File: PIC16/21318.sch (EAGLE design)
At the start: 11 parts, among them U2 I50115

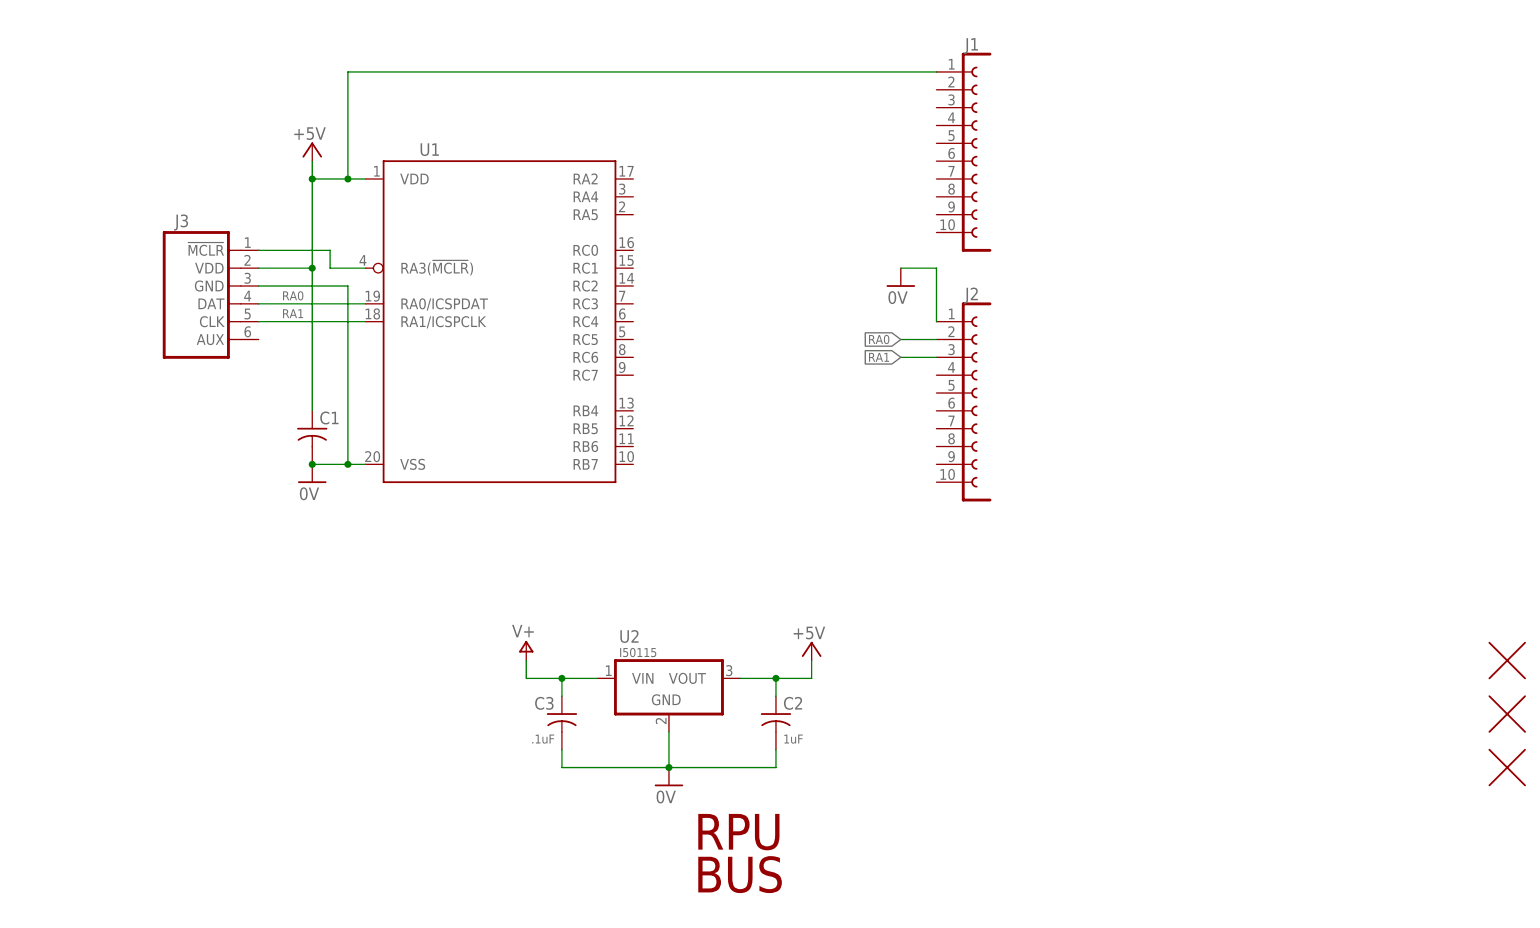
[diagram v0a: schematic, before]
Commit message: PIC16
8pin, 14pin, and 20pin will work, just keep pin 1 fixed.
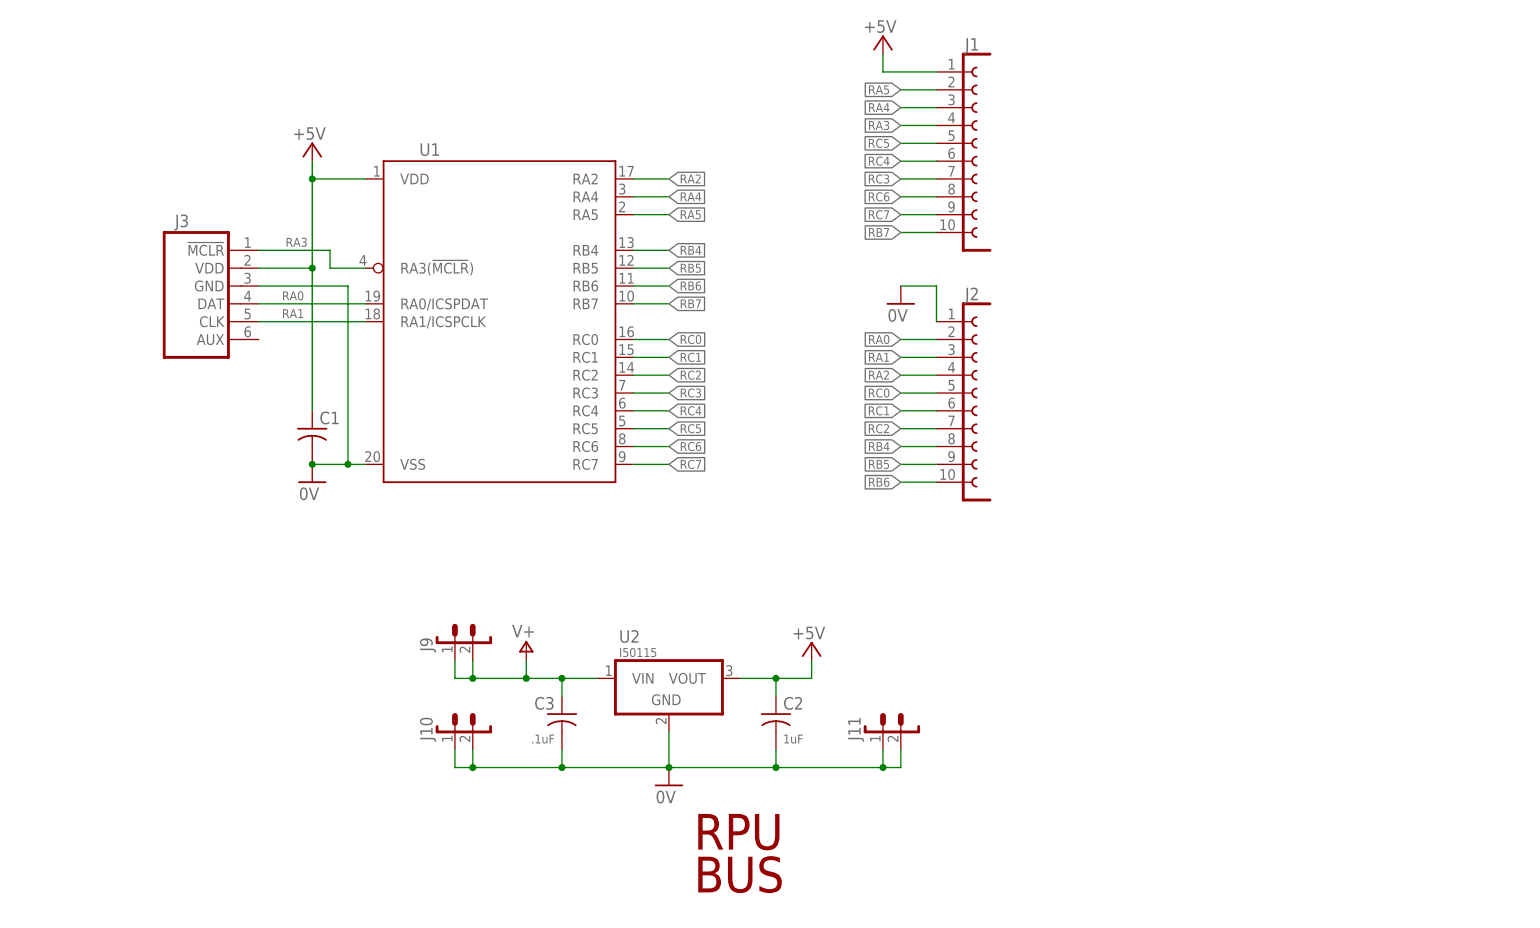
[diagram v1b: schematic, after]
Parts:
- removed U$2, U$3, U$4: FIDUCIAL1.27, H-Fiducial:FIDUCIAL1.27
- added J10, J11, J9: (no value), J-HDR2.54mm:1X2
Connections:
- removed net N$1: J3.!MCLR, U1.RA3(!MCLR!)
- new net RA2: J2.4, U1.RA2
- new net RA3: J1.4, J3.!MCLR, U1.RA3(!MCLR!)
- new net RA4: J1.3, U1.RA4
- new net RA5: J1.2, U1.RA5
- new net RB4: J2.8, U1.RB4
- new net RB5: J2.9, U1.RB5
- new net RB6: J2.10, U1.RB6
- new net RB7: J1.10, U1.RB7
- new net RC0: J2.5, U1.RC0
- new net RC1: J2.6, U1.RC1
- new net RC2: J2.7, U1.RC2
- new net RC3: J1.7, U1.RC3
- new net RC4: J1.6, U1.RC4
- new net RC5: J1.5, U1.RC5
- new net RC6: J1.8, U1.RC6
- new net RC7: J1.9, U1.RC7
- net 0V: now also J10.1, J10.2, J11.1, J11.2
- net V+: now also J9.1, J9.2

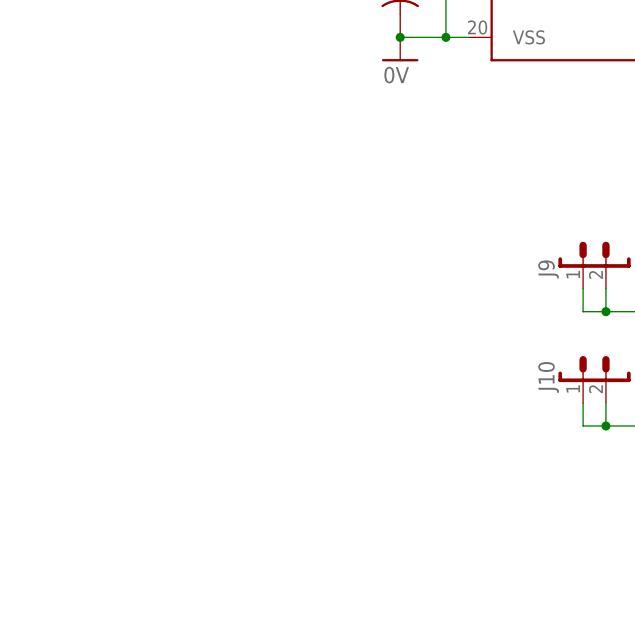
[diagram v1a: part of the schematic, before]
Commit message: PIC16: add three switches
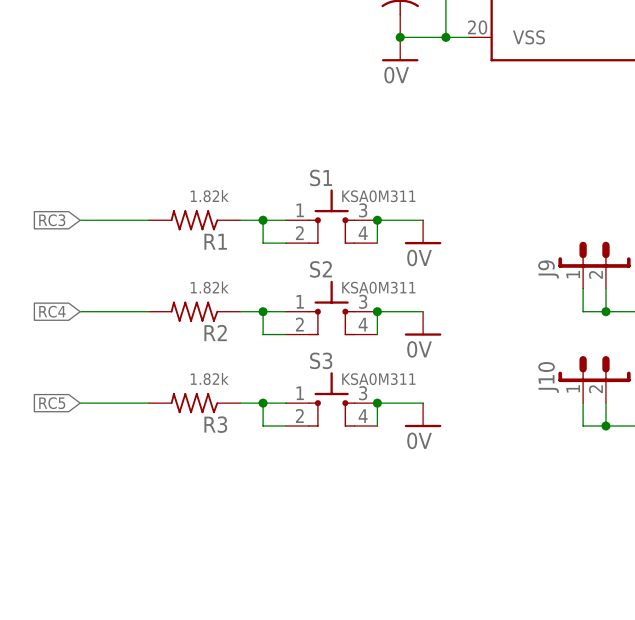
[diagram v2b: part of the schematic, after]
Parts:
- added R1, R2, R3: 1.82k, R-C:R0805
- added S1, S2, S3: KSA0M311, S-Tactile:KSA0M311
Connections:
- new net N$1: R2.1, S2.1, S2.2
- new net N$2: R3.1, S3.1, S3.2
- new net N$93: R1.1, S1.1, S1.2
- net 0V: now also S1.3, S1.4, S2.3, S2.4, S3.3, S3.4
- net RC3: now also R1.2
- net RC4: now also R2.2
- net RC5: now also R3.2
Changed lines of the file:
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@@
 <part name="J10" library="J-HDR2.54mm" deviceset="1X2" device=""/>
 <part name="J11" library="J-HDR2.54mm" deviceset="1X2" device=""/>
+<part name="S1" library="S-Tactile" deviceset="KSA" device="0M311" value="KSA0M311"/>
+<part name="R1" library="R-C" deviceset="R" device="0805" value="1.82k"/>
+<part name="GND61" library="Plane" deviceset="0V" device=""/>
+<part name="S2" library="S-Tactile" deviceset="KSA" device="0M311" value="KSA0M311"/>
+<part name="R2" library="R-C" deviceset="R" device="0805" value="1.82k"/>
+<part name="GND3" library="Plane" deviceset="0V" device=""/>
+<part name="S3" library="S-Tactile" deviceset="KSA" device="0M311" value="KSA0M311"/>
+<part name="R3" library="R-C" deviceset="R" device="0805" value="1.82k"/>
+<part name="GND4" library="Plane" deviceset="0V" device=""/>
 </parts>
 <sheets>
@@
 <instance part="J10" gate="G$1" x="96.52" y="76.2" rot="R90"/>
 <instance part="J11" gate="G$1" x="157.48" y="76.2" rot="R90"/>
+<instance part="S1" gate="S" x="66.04" y="93.98"/>
+<instance part="R1" gate="G$1" x="50.8" y="93.98" rot="R180"/>
+<instance part="GND61" gate="1" x="76.2" y="91.44"/>
+<instance part="S2" gate="S" x="66.04" y="83.82"/>
+<instance part="R2" gate="G$1" x="50.8" y="83.82" rot="R180"/>
+<instance part="GND3" gate="1" x="76.2" y="81.28"/>
+<instance part="S3" gate="S" x="66.04" y="73.66"/>
+<instance part="R3" gate="G$1" x="50.8" y="73.66" rot="R180"/>
+<instance part="GND4" gate="1" x="76.2" y="71.12"/>
 </instances>
 <busses>
@@
 <junction x="73.66" y="114.3"/>
 </segment>
+<segment>
+<pinref part="S1" gate="S" pin="3"/>
+<wire x1="71.12" y1="93.98" x2="76.2" y2="93.98" width="0.1524" layer="91"/>
+<pinref part="GND61" gate="1" pin="0V"/>
+<pinref part="S1" gate="S" pin="4"/>
+<wire x1="71.12" y1="91.44" x2="71.12" y2="93.98" width="0.1524" layer="91"/>
+<junction x="71.12" y="93.98"/>
+</segment>
+<segment>
+<pinref part="S2" gate="S" pin="3"/>
+<wire x1="71.12" y1="83.82" x2="76.2" y2="83.82" width="0.1524" layer="91"/>
+<pinref part="GND3" gate="1" pin="0V"/>
+<pinref part="S2" gate="S" pin="4"/>
+<wire x1="71.12" y1="81.28" x2="71.12" y2="83.82" width="0.1524" layer="91"/>
+<junction x="71.12" y="83.82"/>
+</segment>
+<segment>
+<pinref part="S3" gate="S" pin="3"/>
+<wire x1="71.12" y1="73.66" x2="76.2" y2="73.66" width="0.1524" layer="91"/>
+<pinref part="GND4" gate="1" pin="0V"/>
+<pinref part="S3" gate="S" pin="4"/>
+<wire x1="71.12" y1="71.12" x2="71.12" y2="73.66" width="0.1524" layer="91"/>
+<junction x="71.12" y="73.66"/>
+</segment>
 </net>
 <net name="+5V" class="0">
@@
 <label x="157.48" y="154.94" size="1.27" layer="91" rot="R180" xref="yes"/>
 </segment>
+<segment>
+<pinref part="R1" gate="G$1" pin="2"/>
+<wire x1="45.72" y1="93.98" x2="38.1" y2="93.98" width="0.1524" layer="91"/>
+<label x="38.1" y="93.98" size="1.27" layer="91" rot="R180" xref="yes"/>
+</segment>
 </net>
 <net name="RC5" class="0">
@@
 <label x="157.48" y="160.02" size="1.27" layer="91" rot="R180" xref="yes"/>
 </segment>
+<segment>
+<pinref part="R3" gate="G$1" pin="2"/>
+<wire x1="45.72" y1="73.66" x2="38.1" y2="73.66" width="0.1524" layer="91"/>
+<label x="38.1" y="73.66" size="1.27" layer="91" rot="R180" xref="yes"/>
+</segment>
 </net>
 <net name="RC6" class="0">
@@
 <label x="157.48" y="157.48" size="1.27" layer="91" rot="R180" xref="yes"/>
 </segment>
-</net>
+<segment>
+<pinref part="R2" gate="G$1" pin="2"/>
+<wire x1="45.72" y1="83.82" x2="38.1" y2="83.82" width="0.1524" layer="91"/>
+<label x="38.1" y="83.82" size="1.27" layer="91" rot="R180" xref="yes"/>
+</segment>
+</net>
+<net name="N$93" class="0">
+<segment>
+<pinref part="S1" gate="S" pin="2"/>
+<wire x1="55.88" y1="93.98" x2="58.42" y2="93.98" width="0.1524" layer="91"/>
+<wire x1="58.42" y1="93.98" x2="58.42" y2="91.44" width="0.1524" layer="91"/>
+<wire x1="58.42" y1="91.44" x2="60.96" y2="91.44" width="0.1524" layer="91"/>
+<pinref part="S1" gate="S" pin="1"/>
+<wire x1="60.96" y1="93.98" x2="58.42" y2="93.98" width="0.1524" layer="91"/>
+<junction x="58.42" y="93.98"/>
+<pinref part="R1" gate="G$1" pin="1"/>
+</segment>
+</net>
+<net name="N$1" class="0">
+<segment>
+<pinref part="S2" gate="S" pin="2"/>
+<wire x1="55.88" y1="83.82" x2="58.42" y2="83.82" width="0.1524" layer="91"/>
+<wire x1="58.42" y1="83.82" x2="58.42" y2="81.28" width="0.1524" layer="91"/>
+<wire x1="58.42" y1="81.28" x2="60.96" y2="81.28" width="0.1524" layer="91"/>
+<pinref part="S2" gate="S" pin="1"/>
+<wire x1="60.96" y1="83.82" x2="58.42" y2="83.82" width="0.1524" layer="91"/>
+<junction x="58.42" y="83.82"/>
+<pinref part="R2" gate="G$1" pin="1"/>
+</segment>
+</net>
+<net name="N$2" class="0">
+<segment>
+<pinref part="S3" gate="S" pin="2"/>
+<wire x1="55.88" y1="73.66" x2="58.42" y2="73.66" width="0.1524" layer="91"/>
+<wire x1="58.42" y1="73.66" x2="58.42" y2="71.12" width="0.1524" layer="91"/>
+<wire x1="58.42" y1="71.12" x2="60.96" y2="71.12" width="0.1524" layer="91"/>
+<pinref part="S3" gate="S" pin="1"/>
+<wire x1="60.96" y1="73.66" x2="58.42" y2="73.66" width="0.1524" layer="91"/>
+<junction x="58.42" y="73.66"/>
+<pinref part="R3" gate="G$1" pin="1"/>
+</segment>
+</net>

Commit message: PIC16: schematic
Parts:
- C1: value (none) -> .1uF
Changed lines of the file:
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@@
 <part name="J2" library="J-HDR2.54mm" deviceset="F1X10" device=""/>
 <part name="J3" library="U-PIC" deviceset="ISP" device=""/>
-<part name="C1" library="C-C" deviceset="C" device="C0603A"/>
+<part name="C1" library="C-C" deviceset="C" device="C0603A" value=".1uF"/>
 <part name="C2" library="C-C" deviceset="C" device="C0805A" value="1uF"/>
 <part name="P+1" library="Plane" deviceset="+5V" device=""/>
